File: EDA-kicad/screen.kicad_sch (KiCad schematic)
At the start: 3 parts

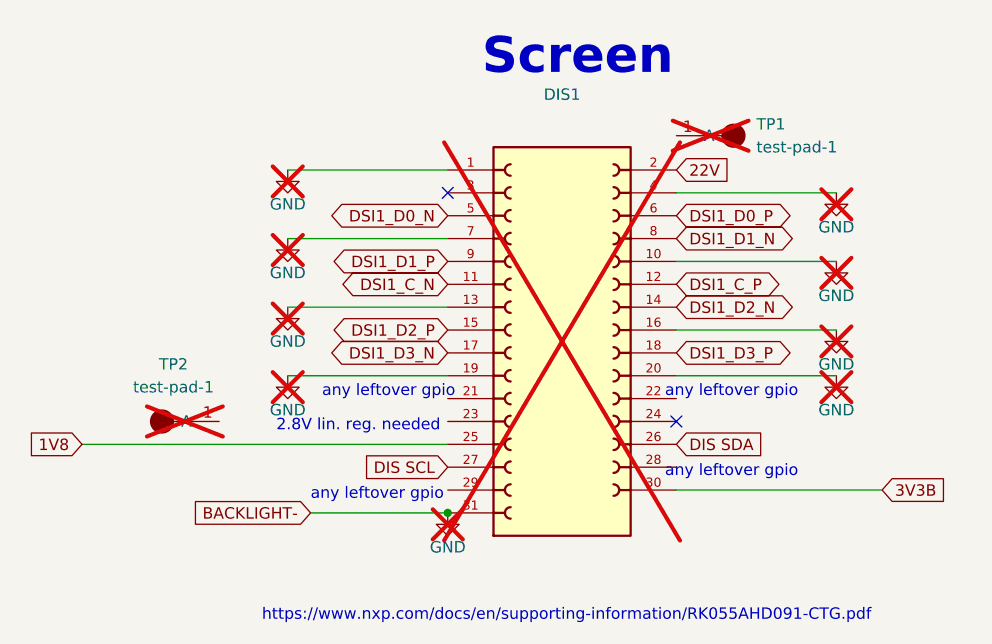
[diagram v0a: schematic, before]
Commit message: screen GND ref
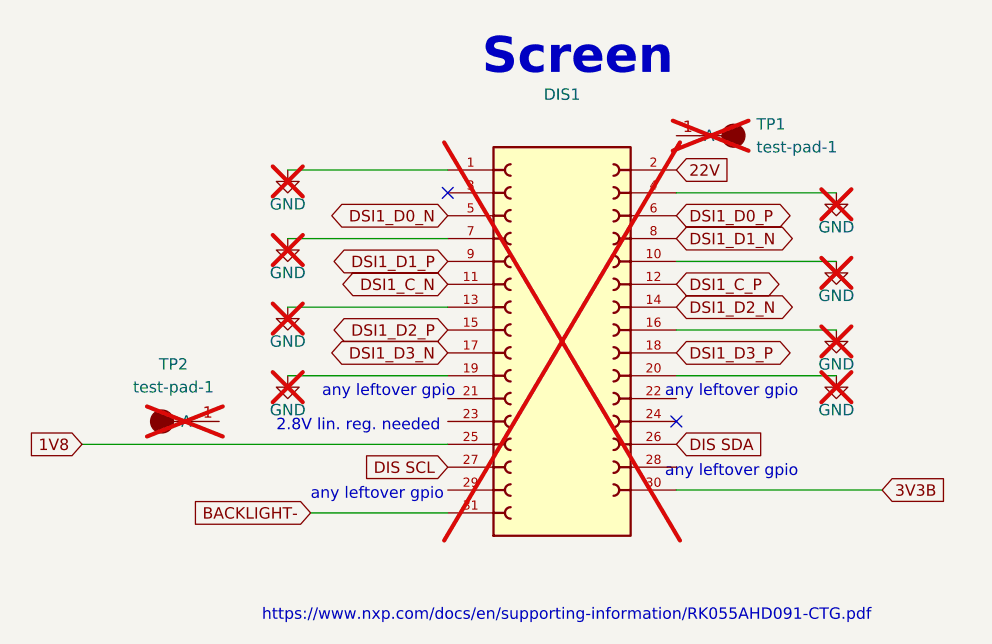
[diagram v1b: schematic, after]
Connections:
- net GND: no longer DIS1.31
- new net BACKLIGHT-: DIS1.31
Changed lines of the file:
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@@
 		)
-	)
-	(junction
-		(at 137.16 110.49)
-		(diameter 0)
-		(color 0 0 0 0)
 	)
 	(no_connect
@@
 					(unit 1)
 				)
-			)
-		)
-	)
-	(symbol
-		(lib_name "GND_6")
-		(lib_id "power:GND")
-		(at 137.16 110.49 0)
-		(unit 1)
-		(exclude_from_sim no)
-		(in_bom yes)
-		(on_board yes)
-		(dnp yes)
-		(property "Reference" "#PWR062"
-			(at 137.16 116.84 0)
-			(effects
-				(font
-					(size 1.27 1.27)
-				)
-				(hide yes)
-			)
-		)
-		(property "Value" "GND"
-			(at 137.16 114.3 0)
-			(effects
-				(font
-					(size 1.27 1.27)
-				)
-			)
-		)
-		(property "Footprint" ""
-			(at 137.16 110.49 0)
-			(effects
-				(font
-					(size 1.27 1.27)
-				)
-				(hide yes)
-			)
-		)
-		(property "Datasheet" ""
-			(at 137.16 110.49 0)
-			(effects
-				(font
-					(size 1.27 1.27)
-				)
-				(hide yes)
-			)
-		)
-		(property "Description" ""
-			(at 137.16 110.49 0)
-			(effects
-				(font
-					(size 1.27 1.27)
-				)
-				(hide yes)
-			)
-		)
-		(pin "1"
-		)
-		(instances
-			(project "cm5-carrier"
-				(path "/28c5e4fe-1ec7-4477-97f0-d2ec1401fad5/02797719-74e3-4dee-b809-c2968ee0cdff"
-					(reference "#PWR062")
-					(unit 1)
-				)
